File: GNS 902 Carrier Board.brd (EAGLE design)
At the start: 36.8 x 25.4 mm, 8 parts, among them U1 GNS-902

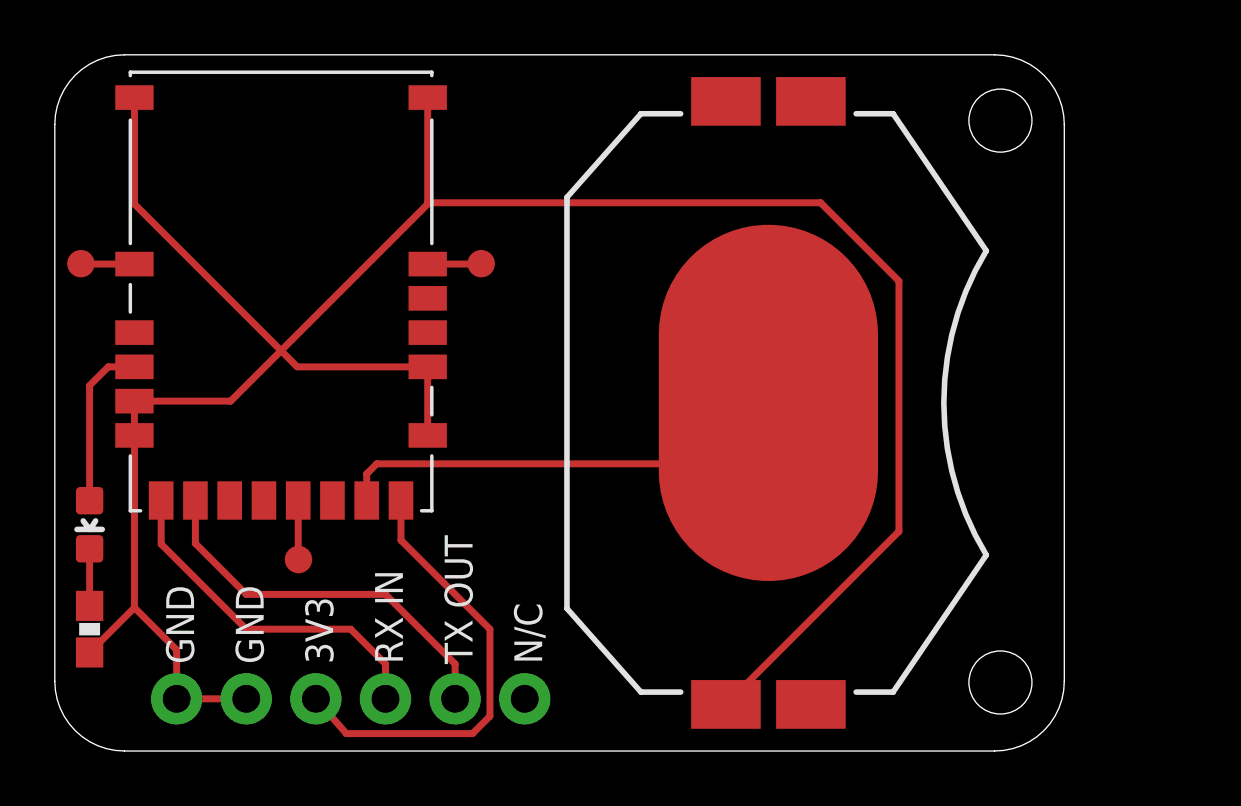
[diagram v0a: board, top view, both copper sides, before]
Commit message: Add automatic VBACKUP power source switch
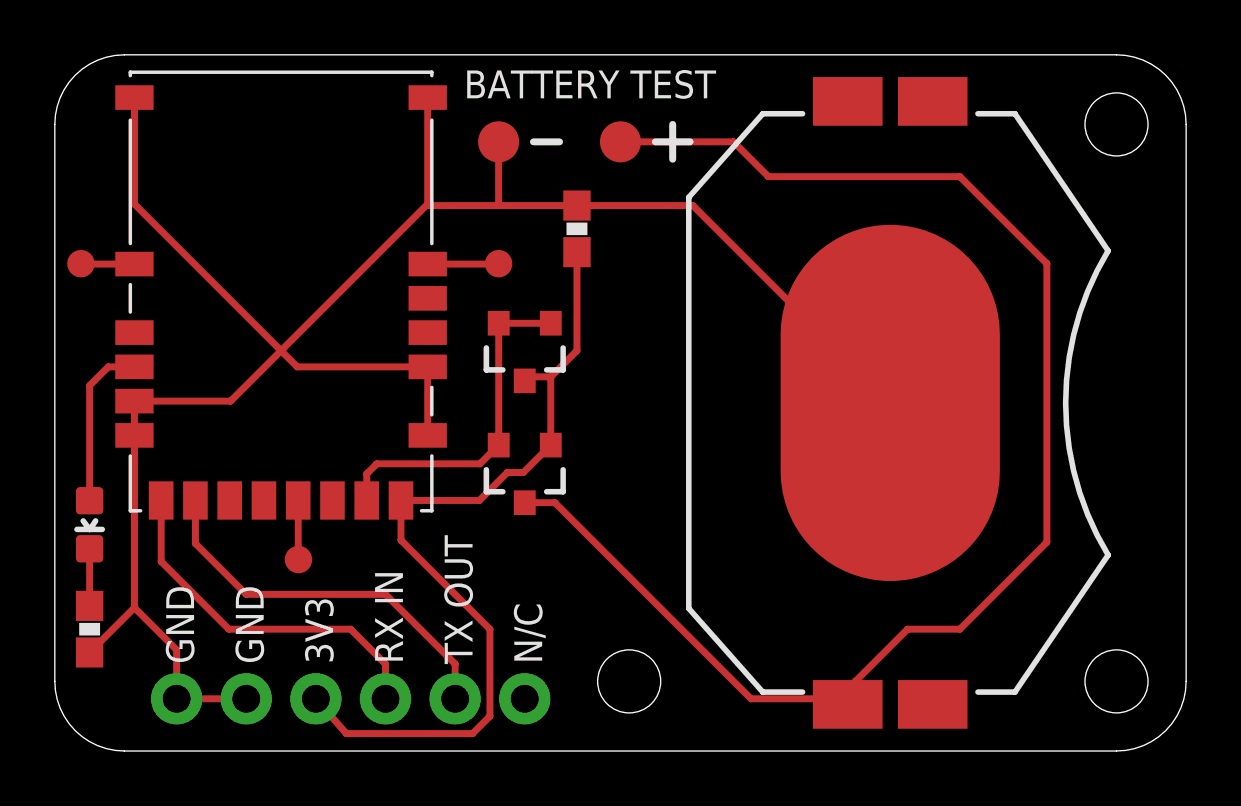
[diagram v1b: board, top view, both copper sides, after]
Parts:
- added Q1, Q2: IRLML6401, SparkFun-DiscreteSemi:SOT23-3
- added R2: 1k, 0603, SparkFun-Resistors:0603-RES
- added TP4, TP5: TPTP10R, testpad:TP10R
- R1: value 47k, 0603 -> 1k, 0603
- TP1, TP2: value TPTP10R -> TPTP15R; device testpad:TP10R -> testpad:TP15R
- moved R1 23.0 mm to (19.1, 19.1), turned to 270 degrees
- moved TP1 20.2 mm to (20.6, 22.2)
- moved TP2 16.9 mm to (16.2, 22.2)
- moved TP3 14.6 mm to (0.95, 17.8)
- moved BAT1 4.45 mm to (30.5, 12.7)
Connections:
- new net N$6: BAT1.1, Q1.3, TP1.TP
- net 3V3: now also Q1.1, Q2.3, R1.2
- net GND: now also BAT1.2, R2.1, TP2.TP; no longer BAT1.1
- net N$2: now also R2.2; no longer R1.2
- net N$3: now also TP3.TP; no longer TP1.TP
- net N$4: now also TP4.TP; no longer TP2.TP
- net N$5: now also TP5.TP; no longer TP3.TP
- net VBATTERY: now also Q1.2, Q2.1, Q2.2; no longer BAT1.2
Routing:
- net N$6: track 0.00 -> 52.4 mm
- net 3V3: track 16.4 -> 31.2 mm
- net GND: track 89.9 -> 75.7 mm
- net VBATTERY: track 16.7 -> 12.6 mm
- net N$5: track 1.96 -> 2.59 mm
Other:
- board size 36.8 x 25.4 mm -> 41.3 x 25.4 mm
- board text added: "BATTERY MUST BE >2V."
- board text added: "BATTERY TEST"
- board text added: "NEW BATTERY LIFE APPROX 1 YEAR."
- board text added: "SETTINGS LOST IF BATTERY REMOVED"
- board text added: "WHEN POWER NOT CONNECTED."
- board text added: "v1.1"
- board text removed: "v1.0"

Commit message: Correct GNS-902 footprint and add notes to schematic
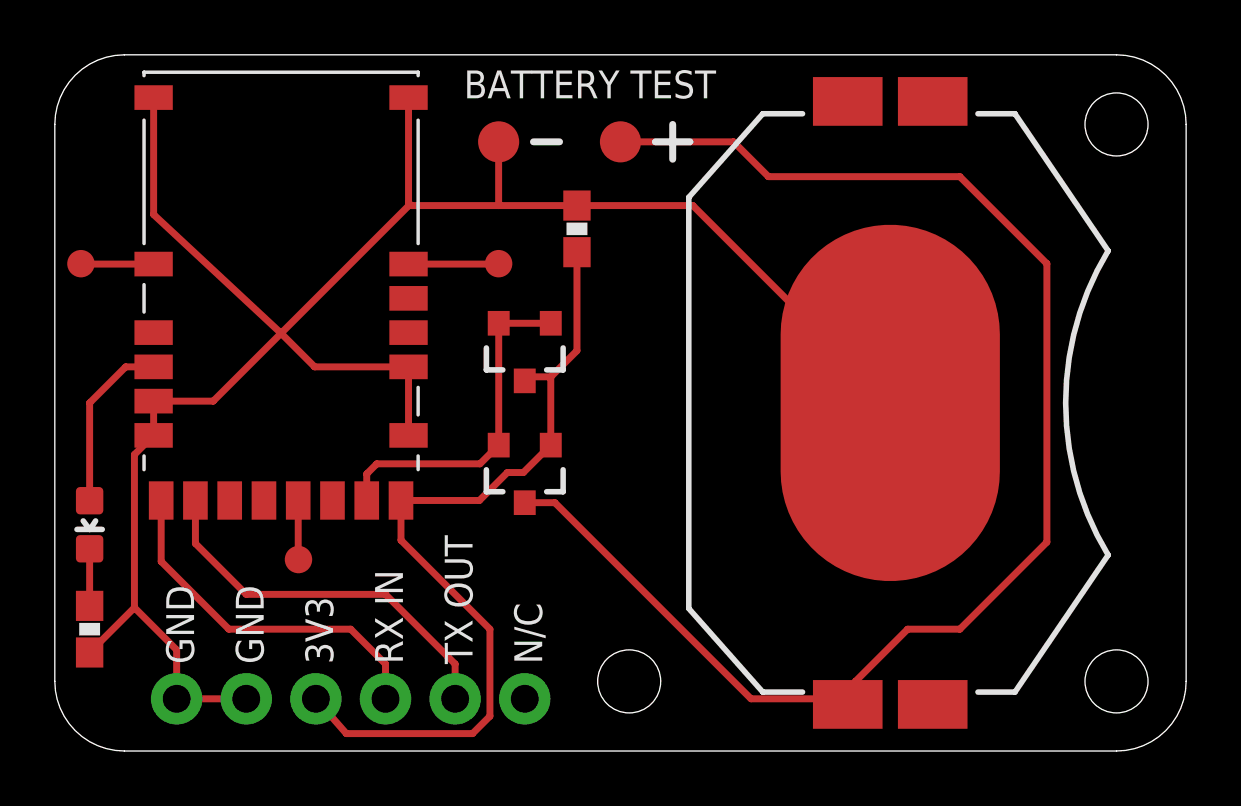
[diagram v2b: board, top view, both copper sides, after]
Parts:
- BAT1: value BAT-HLD-001 -> 20mm coincell
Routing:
- net GND: track 75.7 -> 74.0 mm
- net N$5: track 2.59 -> 3.29 mm
- net N$3: track 1.96 -> 2.66 mm
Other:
- board text added: "v1.2"
- board text removed: "v1.1"
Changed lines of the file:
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@@
 <setting verticaltext="up"/>
 </settings>
-<grid distance="0.025" unitdist="inch" unit="inch" style="dots" multiple="1" display="yes" altdistance="0.025" altunitdist="inch" altunit="inch"/>
+<grid distance="0.0125" unitdist="inch" unit="inch" style="dots" multiple="1" display="yes" altdistance="0.025" altunitdist="inch" altunit="inch"/>
 <layers>
 <layer number="1" name="Top" color="4" fill="1" visible="yes" active="yes"/>
@@
 <text x="17.78" y="3.175" size="1.016" layer="121" font="vector" rot="R90">N/C</text>
 <text x="36.195" y="22.86" size="1.4224" layer="122" font="vector" rot="MR0">GNS 902 Carrier Board</text>
-<text x="36.195" y="20.32" size="1.4224" layer="122" font="vector" rot="MR0">v1.1</text>
+<text x="36.195" y="20.32" size="1.4224" layer="122" font="vector" rot="MR0">v1.2</text>
 <text x="36.195" y="17.78" size="1.4224" layer="122" font="vector" rot="MR0">x-io Technologies Limited</text>
 <text x="14.9225" y="23.8125" size="1.016" layer="121" font="vector">BATTERY TEST</text>
@@
 <element name="R2" library="SparkFun-Resistors" package="0603-RES" value="1k, 0603" x="1.27" y="4.445" smashed="yes" rot="R90"/>
 <element name="U1" library="x-io" package="GNS-902" value="GNS-902" x="8.255" y="24.765" smashed="yes" rot="R180"/>
-<element name="BAT1" library="SparkFun-Electromechanical" package="BATTCON_20MM_4LEGS" value="BAT-HLD-001" x="30.48" y="12.7" smashed="yes" rot="R90">
+<element name="BAT1" library="SparkFun-Electromechanical" package="BATTCON_20MM_4LEGS" value="20mm coincell" x="30.48" y="12.7" smashed="yes" rot="R90">
 <attribute name="PROD_ID" value="BATT-10373" x="30.48" y="12.7" size="1.778" layer="27" rot="R90" display="off"/>
 </element>
@@
 <contactref element="U1" pad="20"/>
 <contactref element="R2" pad="1"/>
-<wire x1="8.255" y1="14.605" x2="8.845" y2="14.015" width="0.254" layer="1"/>
-<wire x1="8.845" y1="14.015" x2="13.605" y2="14.015" width="0.254" layer="1"/>
-<wire x1="2.905" y1="12.765" x2="6.415" y2="12.765" width="0.254" layer="1"/>
-<wire x1="6.415" y1="12.765" x2="8.255" y2="14.605" width="0.254" layer="1"/>
-<wire x1="2.905" y1="11.515" x2="2.905" y2="12.765" width="0.254" layer="1"/>
-<wire x1="13.605" y1="14.015" x2="13.605" y2="11.515" width="0.254" layer="1"/>
-<wire x1="2.905" y1="23.84" x2="2.905" y2="19.955" width="0.254" layer="1"/>
-<wire x1="2.905" y1="19.955" x2="8.255" y2="14.605" width="0.254" layer="1"/>
-<wire x1="13.605" y1="23.84" x2="13.605" y2="19.955" width="0.254" layer="1"/>
-<wire x1="13.605" y1="19.955" x2="8.255" y2="14.605" width="0.254" layer="1"/>
-<wire x1="2.905" y1="11.515" x2="2.905" y2="5.23" width="0.254" layer="1"/>
+<wire x1="8.255" y1="15.24" x2="9.48" y2="14.015" width="0.254" layer="1"/>
+<wire x1="9.48" y1="14.015" x2="12.905" y2="14.015" width="0.254" layer="1"/>
+<wire x1="3.605" y1="12.765" x2="5.78" y2="12.765" width="0.254" layer="1"/>
+<wire x1="5.78" y1="12.765" x2="8.255" y2="15.24" width="0.254" layer="1"/>
+<wire x1="3.605" y1="11.515" x2="3.605" y2="12.765" width="0.254" layer="1"/>
+<wire x1="3.605" y1="19.5725" x2="8.255" y2="15.24" width="0.254" layer="1"/>
+<wire x1="12.905" y1="19.89" x2="8.255" y2="15.24" width="0.254" layer="1"/>
 <wire x1="2.905" y1="5.23" x2="1.27" y2="3.595" width="0.254" layer="1"/>
 <contactref element="JP1" pad="1"/>
@@
 <wire x1="4.445" y1="3.69" x2="2.905" y2="5.23" width="0.254" layer="1"/>
 <contactref element="R1" pad="1"/>
-<wire x1="13.605" y1="19.9" x2="13.605" y2="19.955" width="0.254" layer="1"/>
 <wire x1="19.05" y1="19.9" x2="16.1925" y2="19.9" width="0.254" layer="1"/>
 <contactref element="TP2" pad="TP"/>
-<wire x1="16.1925" y1="19.9" x2="13.605" y2="19.9" width="0.254" layer="1"/>
+<wire x1="16.1925" y1="19.9" x2="13.0075" y2="19.9" width="0.254" layer="1"/>
 <wire x1="16.1925" y1="22.225" x2="16.1925" y2="19.9" width="0.254" layer="1"/>
 <contactref element="BAT1" pad="2"/>
 <wire x1="19.05" y1="19.9" x2="23.28" y2="19.9" width="0.254" layer="1"/>
+<wire x1="3.605" y1="23.84" x2="3.605" y2="19.5725" width="0.254" layer="1"/>
+<wire x1="2.905" y1="5.23" x2="2.905" y2="10.815" width="0.254" layer="1"/>
+<wire x1="2.905" y1="10.815" x2="3.605" y2="11.515" width="0.254" layer="1"/>
+<wire x1="12.905" y1="14.015" x2="12.905" y2="11.515" width="0.254" layer="1"/>
 <wire x1="23.28" y1="19.9" x2="30.48" y2="12.7" width="0.254" layer="1"/>
+<wire x1="12.905" y1="23.84" x2="12.905" y2="20.0025" width="0.254" layer="1"/>
+<wire x1="12.905" y1="20.0025" x2="12.905" y2="19.89" width="0.254" layer="1"/>
+<wire x1="13.0075" y1="19.9" x2="12.905" y2="20.0025" width="0.254" layer="1"/>
 </signal>
 <signal name="N$1">
 <contactref element="U1" pad="4"/>
 <contactref element="D1" pad="A"/>
-<wire x1="1.27" y1="9.132" x2="1.27" y2="13.335" width="0.254" layer="1"/>
-<wire x1="1.27" y1="13.335" x2="1.95" y2="14.015" width="0.254" layer="1"/>
-<wire x1="2.905" y1="14.015" x2="1.95" y2="14.015" width="0.254" layer="1"/>
+<wire x1="1.27" y1="9.132" x2="1.27" y2="12.7" width="0.254" layer="1"/>
+<wire x1="1.27" y1="12.7" x2="2.585" y2="14.015" width="0.254" layer="1"/>
+<wire x1="3.605" y1="14.015" x2="2.585" y2="14.015" width="0.254" layer="1"/>
 </signal>
 <signal name="N$2">
@@
 <contactref element="U1" pad="2"/>
 <contactref element="TP3" pad="TP"/>
-<wire x1="2.905" y1="17.765" x2="0.9675" y2="17.765" width="0.254" layer="1"/>
+<wire x1="3.605" y1="17.765" x2="0.9675" y2="17.765" width="0.254" layer="1"/>
 <wire x1="0.9675" y1="17.765" x2="0.9525" y2="17.78" width="0.254" layer="1"/>
 </signal>
@@
 <contactref element="TP5" pad="TP"/>
 <contactref element="U1" pad="19"/>
-<wire x1="13.605" y1="17.765" x2="16.1775" y2="17.765" width="0.254" layer="1"/>
+<wire x1="12.905" y1="17.765" x2="16.1775" y2="17.765" width="0.254" layer="1"/>
 <wire x1="16.1775" y1="17.765" x2="16.1925" y2="17.78" width="0.254" layer="1"/>
 </signal>
